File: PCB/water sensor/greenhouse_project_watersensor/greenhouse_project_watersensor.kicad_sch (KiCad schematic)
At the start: 28 parts, among them J1 Conn_01x09_Socket, Q1 BC847, Q2 BC847, Q3 BC847, Q4 BC847, Q5 BC847, Q6 BC847, Q7 BC847, Q8 BC847

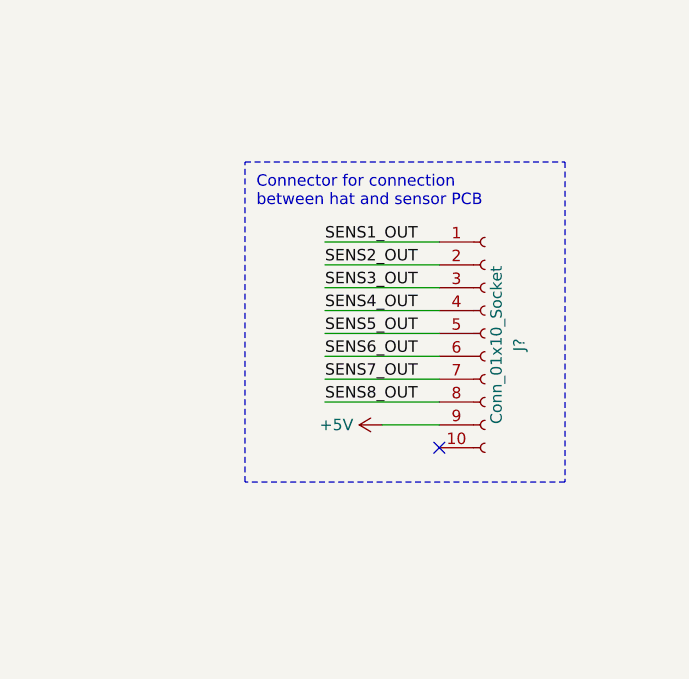
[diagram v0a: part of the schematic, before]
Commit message: Uploaded finals
Pushed the final versions of the microcontroller code, Nodered code, PCB and CAD files to the repository
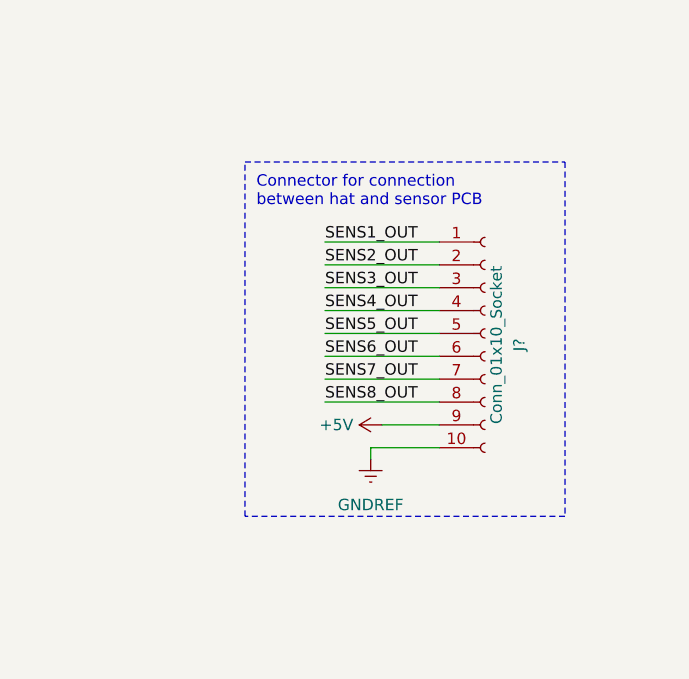
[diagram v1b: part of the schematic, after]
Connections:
- net GNDREF: now also J?.10 (Pin_10)
- no-connect marks 1 -> 0
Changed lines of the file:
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@@
   (title_block
     (title "Greenhouse project FRDM-KL25Z waterlevel sensor")
-    (date "5-7-2023")
+    (date "2023-04-16")
     (rev "V2.0")
     (company "OnlyPlants")
@@
   (junction (at 55.88 59.69) (diameter 0) (color 0 0 0 0)
   )
-  (no_connect (at 226.06 135.89))
   (wire (pts (xy 146.05 97.79) (xy 146.05 99.06))
     (stroke (width 0) (type default))
@@
     (stroke (width 0) (type default))
   )
+  (wire (pts (xy 218.44 135.89) (xy 226.06 135.89))
+    (stroke (width 0) (type default))
+  )
   (wire (pts (xy 71.12 99.06) (xy 55.88 99.06))
     (stroke (width 0) (type default))
@@
   )
   (wire (pts (xy 130.81 151.13) (xy 143.51 151.13))
+    (stroke (width 0) (type default))
+  )
+  (wire (pts (xy 218.44 137.16) (xy 218.44 135.89))
     (stroke (width 0) (type default))
   )
@@
     (fill (type none))
   )
-  (rectangle (start 204.47 104.14) (end 240.03 139.7)
+  (rectangle (start 204.47 104.14) (end 240.03 143.51)
     (stroke (width 0) (type dash))
     (fill (type none))
@@
         )
       )
+    )
+  )
+  (symbol (lib_id "power:GNDREF") (at 218.44 137.16 0) (unit 1)
+    (in_bom yes) (on_board yes) (dnp no) (fields_autoplaced)
+    (property "Reference" "#PWR020" (at 218.44 143.51 0)
+      (effects (font (size 1.27 1.27)) hide)
+    )
+    (property "Value" "GNDREF" (at 218.44 142.24 0)
+      (effects (font (size 1.27 1.27)))
+    )
+    (property "Footprint" "" (at 218.44 137.16 0)
+      (effects (font (size 1.27 1.27)) hide)
+    )
+    (property "Datasheet" "" (at 218.44 137.16 0)
+      (effects (font (size 1.27 1.27)) hide)
+    )
+    (pin "1")
+    (instances
+      (project "greenhouse_project_watersensor"
+        (path "/85ace96d-2557-4ab4-a42b-9b438c6d3f6f"
+          (reference "#PWR020") (unit 1)
+        )
+      )
+      (project "greenhouse_project_hat"
+        (path "/b27d5451-0104-43eb-badd-cec4b3afa639/4d8eb8bd-7658-4ee1-a9bd-e11f7f5e7e34"
+          (reference "#PWR?") (unit 1)
+        )
+        (path "/b27d5451-0104-43eb-badd-cec4b3afa639/14bbbbaf-372e-4e9f-862e-9e90fad91d90"
+          (reference "#PWR068") (unit 1)
+        )
+      )
